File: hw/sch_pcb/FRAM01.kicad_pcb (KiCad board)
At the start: 2 copper layers, 19.8 x 30 mm, 9 parts, among them IC1 CY15B108QN-40SXI, J2 HEADER_2x04, M1 HOLE M3, M2 HOLE M3, M3 HOLE, M4 HOLE

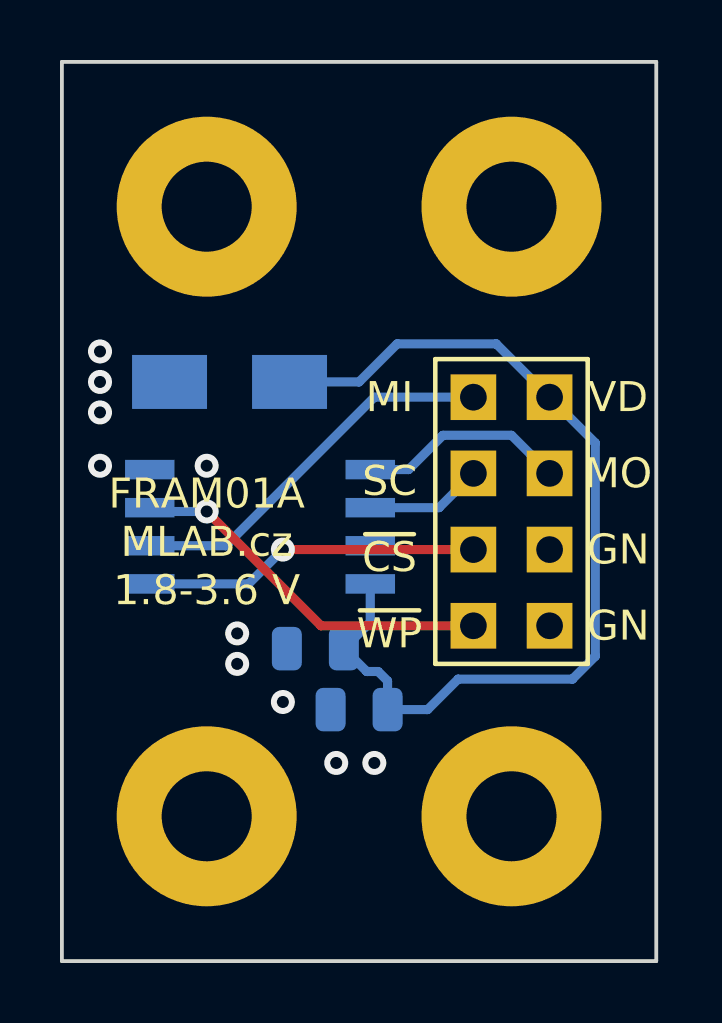
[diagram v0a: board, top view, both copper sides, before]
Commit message: change zener diode, minor improvements in silkscreen
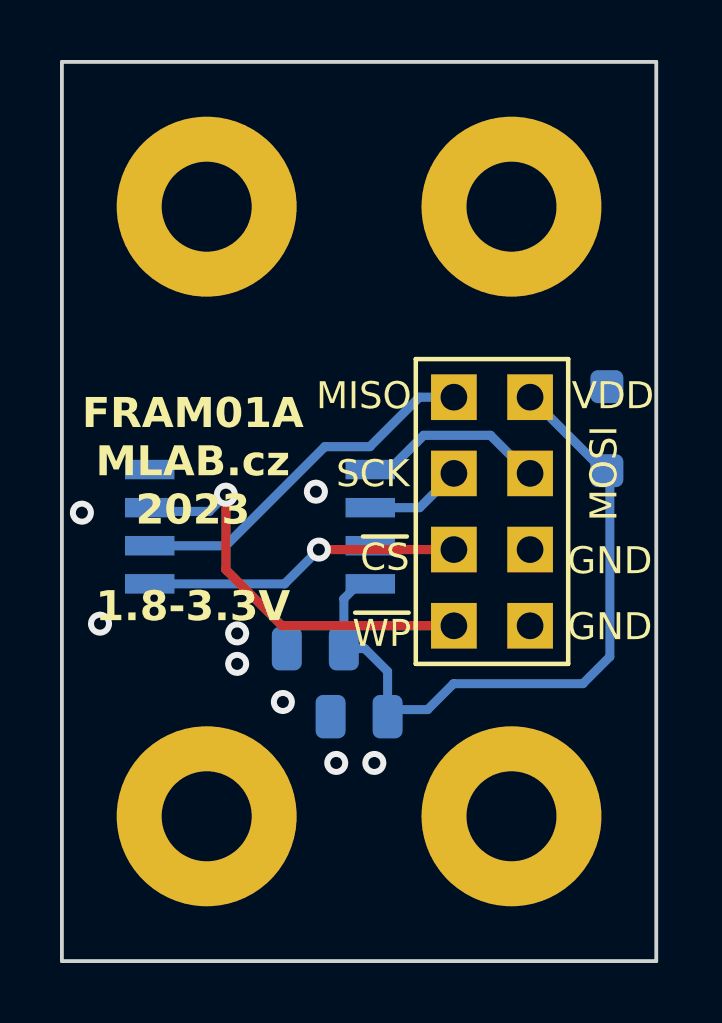
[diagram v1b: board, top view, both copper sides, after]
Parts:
- D1: value BZV55C-5,6V -> BZT52H-C3V6,115; footprint Diode_SMD:D_SMA -> Diode_SMD:D_SOD-123F
- moved D1 12.7 mm to (150.5, 83.6), turned to 90 degrees
- moved J2 0.65 mm to (146.7, 86.4)
- moved C1 0.24 mm to (142.2, 93.2)
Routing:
- net +3.3V: track 32.2 -> 23.0 mm
- net ~{WP}: track 12.4 -> 13.7 mm
- net MOSI: track 6.98 -> 6.28 mm
- net MISO: track 12.8 -> 12.2 mm
- net ~{CS}: track 11.3 -> 10.6 mm
- net SCK: track 3.91 -> 3.26 mm
- net GND: vias 10 -> 8
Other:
- board text added: "FRAM01A MLAB.cz 2023 1.8-3.3V"
- board text added: "GND"
- board text added: "MISO"
- board text added: "MOSI"
- board text added: "SCK"
- board text added: "VDD"
- board text removed: "FRAM01A MLAB.cz 1.8-3.6 V"
- board text removed: "GN"
- board text removed: "MI"
- board text removed: "MO"
- board text removed: "SC"
- board text removed: "VD"

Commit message: add fiducial
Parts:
- added FID1: Fiducial, Fiducial:Fiducial_1mm_Mask2mm, B.Cu at (142.0, 97.0)
- added FID2: Fiducial, Fiducial:Fiducial_1mm_Mask2mm, B.Cu at (140.0, 80.0)
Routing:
- net ~{WP}: track 13.7 -> 12.3 mm
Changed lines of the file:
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@@
     )
+  )
+  (footprint "Fiducial:Fiducial_1mm_Mask2mm" (layer "B.Cu")
+    (at 140 80 180)
+    (descr "Circular Fiducial, 1mm bare copper, 2mm soldermask opening (Level A)")
+    (tags "fiducial")
+    (property "Sheetfile" "FRAM01.kicad_sch")
+    (property "Sheetname" "")
+    (property "ki_description" "Fiducial Marker")
+    (property "ki_keywords" "fiducial marker")
+    (attr smd)
+    (fp_text reference "FID2" (at 0 2) (layer "B.SilkS") hide
+        (effects (font (size 1 1) (thickness 0.15)) (justify mirror))
+    )
+    (fp_text value "Fiducial" (at 0 -2) (layer "B.Fab")
+        (effects (font (size 1 1) (thickness 0.15)) (justify mirror))
+    )
+    (fp_text user "${REFERENCE}" (at 0 0) (layer "B.Fab")
+        (effects (font (size 0.4 0.4) (thickness 0.06)) (justify mirror))
+    )
+    (fp_circle (center 0 0) (end 1.25 0)
+      (stroke (width 0.05) (type solid)) (fill none) (layer "B.CrtYd"))
+    (fp_circle (center 0 0) (end 1 0)
+      (stroke (width 0.1) (type solid)) (fill none) (layer "B.Fab"))
+    (pad "" smd circle (at 0 0 180) (size 1 1) (layers "B.Cu" "B.Mask")
+      (solder_mask_margin 0.5) (clearance 0.5))
+  )
+  (footprint "Fiducial:Fiducial_1mm_Mask2mm" (layer "B.Cu")
+    (at 142 97 180)
+    (descr "Circular Fiducial, 1mm bare copper, 2mm soldermask opening (Level A)")
+    (tags "fiducial")
+    (property "Sheetfile" "FRAM01.kicad_sch")
+    (property "Sheetname" "")
+    (property "ki_description" "Fiducial Marker")
+    (property "ki_keywords" "fiducial marker")
+    (attr smd exclude_from_bom)
+    (fp_text reference "FID1" (at 0 2) (layer "B.SilkS") hide
+        (effects (font (size 1 1) (thickness 0.15)) (justify mirror))
+    )
+    (fp_text value "Fiducial" (at 0 -2) (layer "B.Fab")
+        (effects (font (size 1 1) (thickness 0.15)) (justify mirror))
+    )
+    (fp_text user "${REFERENCE}" (at 0 0) (layer "B.Fab")
+        (effects (font (size 0.4 0.4) (thickness 0.06)) (justify mirror))
+    )
+    (fp_circle (center 0 0) (end 1.25 0)
+      (stroke (width 0.05) (type solid)) (fill none) (layer "B.CrtYd"))
+    (fp_circle (center 0 0) (end 1 0)
+      (stroke (width 0.1) (type solid)) (fill none) (layer "B.Fab"))
+    (pad "" smd circle (at 0 0 180) (size 1 1) (layers "B.Cu" "B.Mask")
+      (solder_mask_margin 0.5) (clearance 0.5))
   )
   (footprint "Capacitor_SMD:C_0805_2012Metric" (layer "B.Cu")
@@
   (segment (start 140.9 87.63) (end 139.757 88.773) (width 0.3048) (layer "B.Cu") (net 2))
   (segment (start 139.757 88.773) (end 135.263 88.773) (width 0.3048) (layer "B.Cu") (net 2))
-  (segment (start 135.263 87.503) (end 137.795 87.503) (width 0.3048) (layer "B.Cu") (net 3))
-  (segment (start 137.795 87.503) (end 141.098 84.2) (width 0.3048) (layer "B.Cu") (net 3))
-  (segment (start 144.25 82.55) (end 145.4 82.55) (width 0.3048) (layer "B.Cu") (net 3))
-  (segment (start 141.098 84.2) (end 142.6 84.2) (width 0.3048) (layer "B.Cu") (net 3))
-  (segment (start 142.6 84.2) (end 144.25 82.55) (width 0.3048) (layer "B.Cu") (net 3))
-  (segment (start 137.8 88.3) (end 139.67 90.17) (width 0.3048) (layer "F.Cu") (net 4))
+  (segment (start 135.263 87.503) (end 137.397 87.503) (width 0.3048) (layer "B.Cu") (net 3))
+  (segment (start 137.397 87.503) (end 142.35 82.55) (width 0.3048) (layer "B.Cu") (net 3))
+  (segment (start 142.35 82.55) (end 145.4 82.55) (width 0.3048) (layer "B.Cu") (net 3))
+  (segment (start 136.8 86.36) (end 136.8 87.3) (width 0.3048) (layer "F.Cu") (net 4))
+  (segment (start 136.8 87.3) (end 139.67 90.17) (width 0.3048) (layer "F.Cu") (net 4))
   (segment (start 139.67 90.17) (end 145.4 90.17) (width 0.3048) (layer "F.Cu") (net 4))
-  (segment (start 137.8 85.8) (end 137.8 88.3) (width 0.3048) (layer "F.Cu") (net 4))
-  (via (at 137.8 85.8) (size 0.8) (drill 0.4) (layers "F.Cu" "B.Cu") (net 4))
-  (segment (start 137.24 86.36) (end 135.39 86.36) (width 0.3048) (layer "B.Cu") (net 4))
-  (segment (start 137.8 85.8) (end 137.24 86.36) (width 0.3048) (layer "B.Cu") (net 4))
+  (via (at 136.8 86.36) (size 0.8) (drill 0.4) (layers "F.Cu" "B.Cu") (net 4))
+  (segment (start 136.8 86.36) (end 135.39 86.36) (width 0.3048) (layer "B.Cu") (net 4))
   (segment (start 135.39 86.36) (end 135.263 86.233) (width 0.25) (layer "B.Cu") (net 4))
   (segment (start 146.62 83.82) (end 147.89 85.09) (width 0.3048) (layer "B.Cu") (net 5))

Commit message: Split silkscreen to avoid collision with vias. Update title-block
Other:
- board text added: "1.8-3.3V"
- board text added: "FRAM01A MLAB.cz 2023"
- board text removed: "FRAM01A MLAB.cz 2023 1.8-3.3V"
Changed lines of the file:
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@@
     (effects (font (size 0.9 0.9) (thickness 0.15)))
   )
-  (gr_text "FRAM01A\nMLAB.cz\n2023\n\n1.8-3.3V" (at 136.7 86.3) (layer "F.SilkS")
+  (gr_text "FRAM01A\nMLAB.cz\n2023" (at 136.8 85.56) (layer "F.SilkS")
     (effects (font (size 1 1) (thickness 0.2) bold))
   )
@@
     (effects (font (size 0.9 0.9) (thickness 0.15)))
   )
+  (gr_text "1.8-3.3V" (at 142.81 80.38 90) (layer "F.SilkS")
+    (effects (font (size 0.9 0.9) (thickness 0.15)) (justify left bottom))
+  )
   (gr_text "MOSI" (at 150.4 85.09 90) (layer "F.SilkS")

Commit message: power connection added, SPI connector changed, cherrypick, simple repairs
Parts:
- added J1: HEADER_2x03_PARALLEL, Connector_PinHeader_2.54mm:PinHeader_2x03_P2.54mm_Vertical, F.Cu at (139.4, 81.6)
- J2: footprint Mlab_Pin_Headers:Straight_2x04 -> Connector_PinHeader_2.54mm:PinHeader_2x04_P2.54mm_Vertical
- moved J2 4.05 mm to (145.3, 82.5)
- moved FID2 2.68 mm to (142.2, 78.5)
- moved C1 1.72 mm to (142.3, 94.9), turned to -90 degrees
- moved IC1 1.65 mm to (138.1, 88.3)
- moved FID1 1.54 mm to (142.2, 98.5)
- moved C2 1.32 mm to (141.1, 92.2)
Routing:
- net +3.3V: track 23.0 -> 37.6 mm
- net ~{WP}: track 12.3 -> 14.7 mm
- net ~{CS}: track 10.6 -> 12.3 mm
- net SCK: track 3.26 -> 4.72 mm
- net MISO: track 12.2 -> 13.6 mm
- net GND: track 0.00 -> 1.41 mm, vias 8 -> 1
- net MOSI: track 6.28 -> 7.68 mm

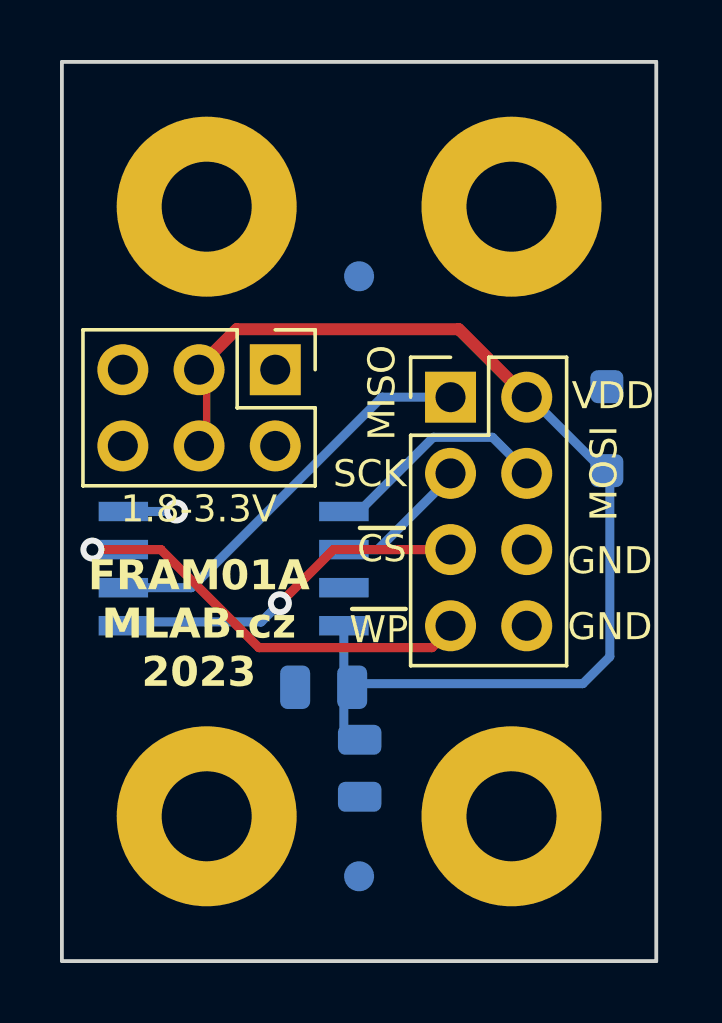
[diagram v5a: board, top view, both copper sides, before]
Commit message: Kontrola a upravy PCB pred vyrobou
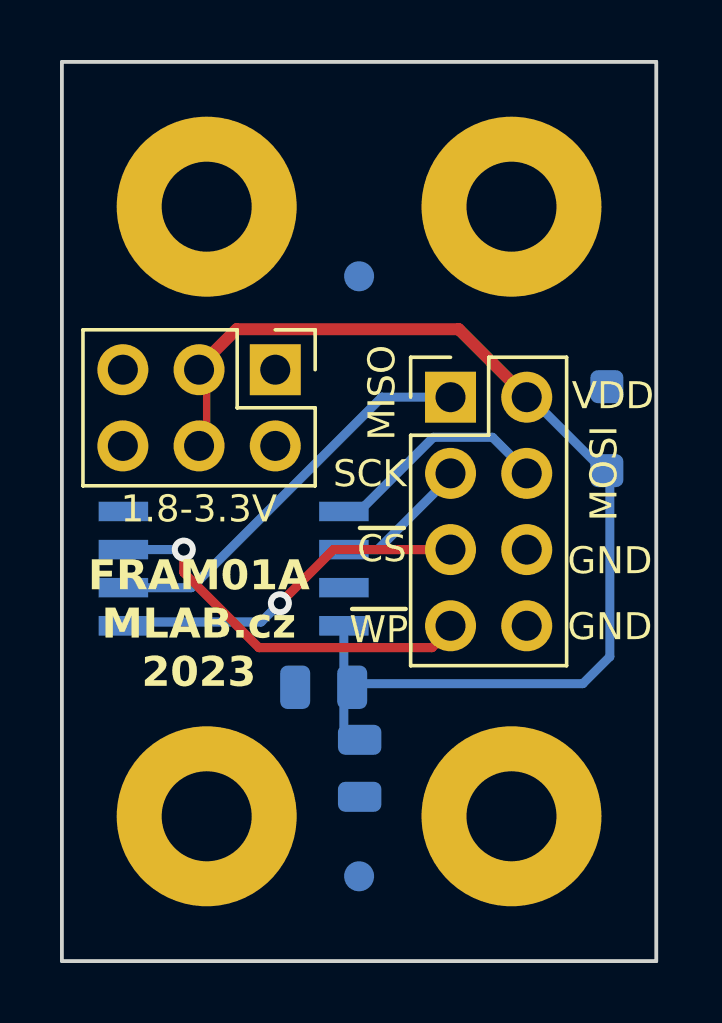
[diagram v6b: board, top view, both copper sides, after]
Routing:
- net ~{WP}: track 14.7 -> 13.1 mm
- net GND: track 1.41 -> 0.00 mm, vias 1 -> 0
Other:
- rule pad_to_mask_clearance: 0 -> 0.2
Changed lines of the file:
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@@
   )
   (setup
-    (pad_to_mask_clearance 0)
+    (stackup
+      (layer "F.SilkS" (type "Top Silk Screen"))
+      (layer "F.Paste" (type "Top Solder Paste"))
+      (layer "F.Mask" (type "Top Solder Mask") (thickness 0.01))
+      (layer "F.Cu" (type "copper") (thickness 0.035))
+      (layer "dielectric 1" (type "core") (thickness 1.51) (material "FR4") (epsilon_r 4.5) (loss_tangent 0.02))
+      (layer "B.Cu" (type "copper") (thickness 0.035))
+      (layer "B.Mask" (type "Bottom Solder Mask") (thickness 0.01))
+      (layer "B.Paste" (type "Bottom Solder Paste"))
+      (layer "B.SilkS" (type "Bottom Silk Screen"))
+      (copper_finish "None")
+      (dielectric_constraints no)
+    )
+    (pad_to_mask_clearance 0.2)
     (aux_axis_origin 137.16 96.52)
     (grid_origin 137.16 96.52)
@@
     (pad "1" thru_hole circle (at 0 0) (size 6 6) (drill 3) (layers "*.Cu" "*.Mask")
       (net 1 "GND") (pintype "input") (clearance 1) (zone_connect 2))
-    (model "${MLAB}/src/3d/mechanical/m3_komplet.step"
-      (offset (xyz 0 0 0))
-      (scale (xyz 1 1 1))
-      (rotate (xyz 0 0 0))
+    (model "${MLAB_3DMODEL_DIR}/DIN_912-M3x10.stp"
+      (offset (xyz 0 0 0))
+      (scale (xyz 1 1 1))
+      (rotate (xyz 0 -90 0))
     )
   )
@@
     (pad "1" thru_hole circle (at 0 0) (size 6 6) (drill 3) (layers "*.Cu" "*.Mask")
       (net 1 "GND") (pintype "input") (clearance 1) (zone_connect 2))
-    (model "${MLAB}/src/3d/mechanical/m3_komplet.step"
-      (offset (xyz 0 0 0))
-      (scale (xyz 1 1 1))
-      (rotate (xyz 0 0 0))
+    (model "${MLAB_3DMODEL_DIR}/DIN_912-M3x10.stp"
+      (offset (xyz 0 0 0))
+      (scale (xyz 1 1 1))
+      (rotate (xyz 0 -90 0))
     )
   )
@@
     (pad "1" thru_hole circle (at 0 0) (size 6 6) (drill 3) (layers "*.Cu" "*.Mask")
       (net 1 "GND") (pintype "input") (clearance 1) (zone_connect 2))
-    (model "${MLAB}/src/3d/mechanical/m3_komplet.step"
-      (offset (xyz 0 0 0))
-      (scale (xyz 1 1 1))
-      (rotate (xyz 0 0 0))
+    (model "${MLAB_3DMODEL_DIR}/DIN_912-M3x10.stp"
+      (offset (xyz 0 0 0))
+      (scale (xyz 1 1 1))
+      (rotate (xyz 0 -90 0))
     )
   )
@@
     (pad "1" thru_hole circle (at 0 0) (size 6 6) (drill 3) (layers "*.Cu" "*.Mask")
       (net 1 "GND") (pintype "input") (clearance 1) (zone_connect 2))
-    (model "${MLAB}/src/3d/mechanical/m3_komplet.step"
-      (offset (xyz 0 0 0))
-      (scale (xyz 1 1 1))
-      (rotate (xyz 0 0 0))
+    (model "${MLAB_3DMODEL_DIR}/DIN_912-M3x10.stp"
+      (offset (xyz 0 0 0))
+      (scale (xyz 1 1 1))
+      (rotate (xyz 0 -90 0))
     )
   )
@@
     (style (thickness 0.15) (arrow_length 1.27) (text_position_mode 0) (extension_height 0.58642) (extension_offset 0.5) keep_text_aligned)
   )
-  (via (at 136.144 86.36) (size 0.8) (drill 0.4) (layers "F.Cu" "B.Cu") (net 1))
-  (segment (start 136.144 86.36) (end 134.734 86.36) (width 0.3048) (layer "B.Cu") (net 1))
   (segment (start 141.3881 87.63) (end 145.4 87.63) (width 0.3048) (layer "F.Cu") (net 2))
   (segment (start 139.6 89.4181) (end 141.3881 87.63) (width 0.3048) (layer "F.Cu") (net 2))
@@
   (segment (start 136.652 88.9) (end 143.002 82.55) (width 0.3048) (layer "B.Cu") (net 3))
   (segment (start 143.002 82.55) (end 145.4 82.55) (width 0.3048) (layer "B.Cu") (net 3))
-  (segment (start 133.35 87.63) (end 135.636 87.63) (width 0.3048) (layer "F.Cu") (net 4))
+  (segment (start 138.906 90.9) (end 144.67 90.9) (width 0.3048) (layer "F.Cu") (net 4))
   (segment (start 144.67 90.9) (end 145.4 90.17) (width 0.3048) (layer "F.Cu") (net 4))
-  (segment (start 138.906 90.9) (end 144.67 90.9) (width 0.3048) (layer "F.Cu") (net 4))
-  (segment (start 135.636 87.63) (end 138.906 90.9) (width 0.3048) (layer "F.Cu") (net 4))
-  (via (at 133.35 87.63) (size 0.8) (drill 0.4) (layers "F.Cu" "B.Cu") (net 4))
-  (segment (start 134.382 87.63) (end 133.35 87.63) (width 0.25) (layer "B.Cu") (net 4))
+  (segment (start 136.398 88.392) (end 138.906 90.9) (width 0.3048) (layer "F.Cu") (net 4))
+  (segment (start 136.398 87.63) (end 136.398 88.392) (width 0.3048) (layer "F.Cu") (net 4))
+  (via (at 136.398 87.63) (size 0.8) (drill 0.4) (layers "F.Cu" "B.Cu") (net 4))
+  (segment (start 134.382 87.63) (end 136.398 87.63) (width 0.3048) (layer "B.Cu") (net 4))
   (segment (start 142.24 86.36) (end 144.7124 83.8876) (width 0.3048) (layer "B.Cu") (net 5))
   (segment (start 146.6876 83.8876) (end 147.89 85.09) (width 0.3048) (layer "B.Cu") (net 5))
